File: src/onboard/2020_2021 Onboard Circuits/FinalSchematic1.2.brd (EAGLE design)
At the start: 135.6 x 80 mm, 97 parts, among them IC1 A5975D, IC2 A5975D, IC3 A5975D

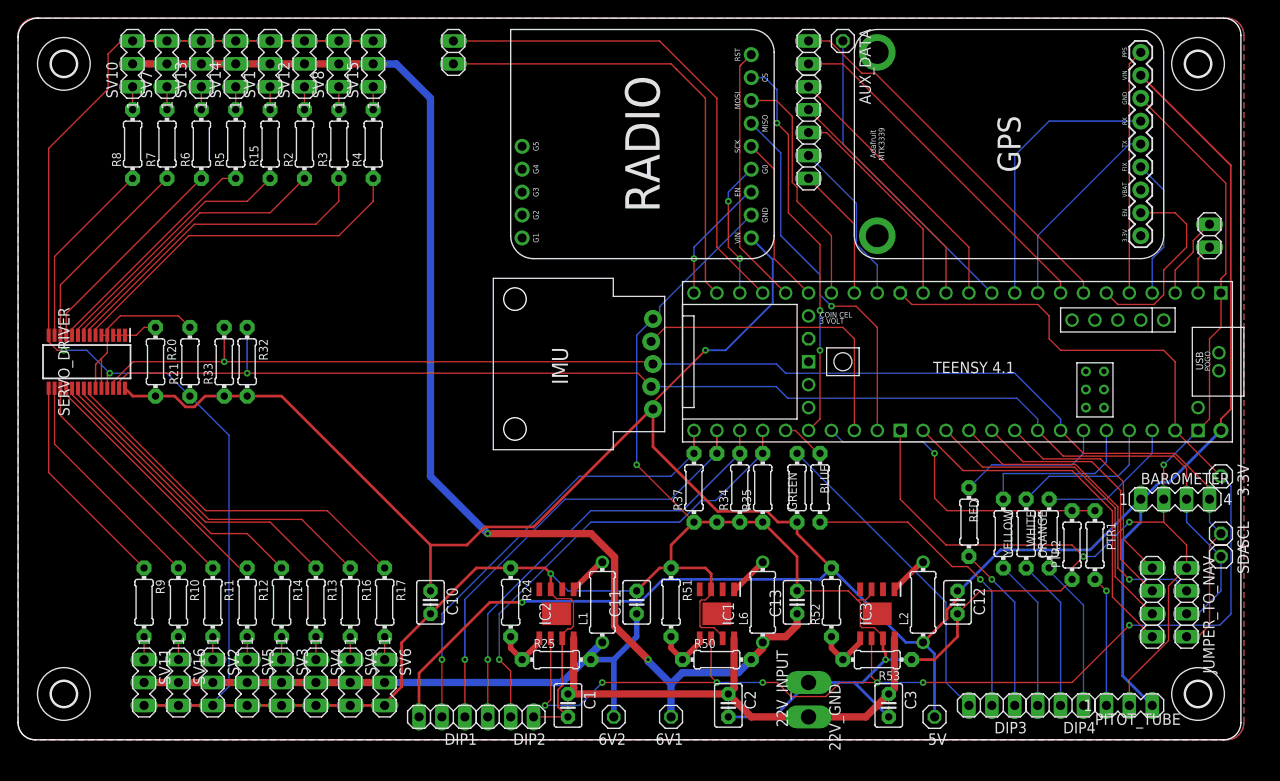
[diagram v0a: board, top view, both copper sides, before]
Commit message: Updated board using the jlcpcb2layer.dru file for DRC check. Added names next to pinheaders. Adjusted silkscreen of component names. Updated photos of baord and schematic.
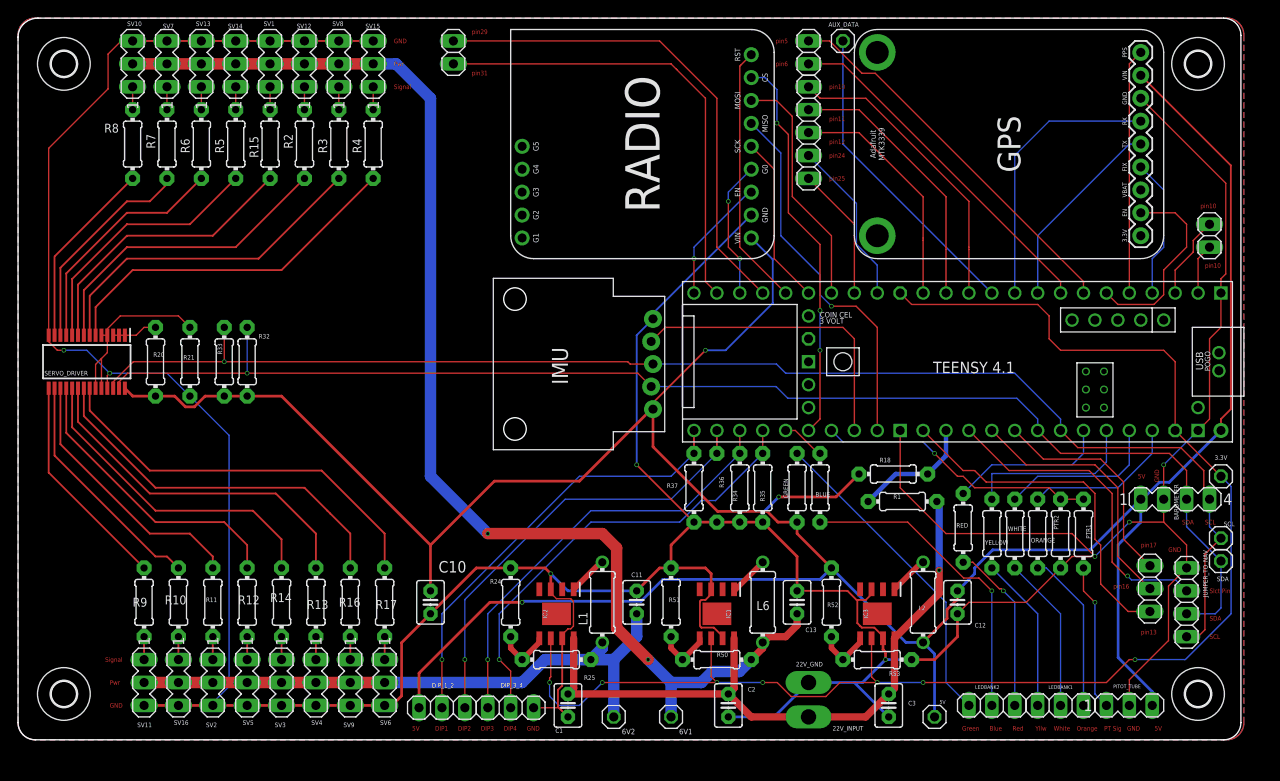
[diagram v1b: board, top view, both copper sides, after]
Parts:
- removed 3: (no value), pinhead:1X04
- removed DIP1, DIP2: (no value), pinhead:1X03
- added DIP_1_2, DIP_3_4, JP1: (no value), pinhead:1X03
- added R1: 1.8M, adafruit:0204/7
- added R18: 430k, adafruit:0204/7
- moved PTR1 1.80 mm to (82.5, 22.9)
- moved PTR2 1.80 mm to (80.0, 22.9)
- moved ORANGE 1.27 mm to (77.5, 22.9)
- moved WHITE 1.27 mm to (74.9, 22.9)
- moved YELLOW 1.27 mm to (72.4, 22.9)
- moved RED 0.90 mm to (69.2, 23.5)
- moved SCL 0.51 mm to (97.8, 22.4)
- moved SDA 0.51 mm to (97.8, 19.8)
- renumbered DIP3 to LEDBANK2, DIP4 to LEDBANK1
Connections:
- net 22_INPUT: now also R1.2
- net 5V: now also DIP_1_2.3; no longer DIP1.3
- net DIP1: now also DIP_1_2.2; no longer DIP1.2
- net DIP2: now also DIP_1_2.1; no longer DIP1.1
- net DIP3: now also DIP_3_4.3; no longer DIP2.3
- net DIP4: now also DIP_3_4.2; no longer DIP2.2
- net GND: now also DIP_3_4.1, R18.1; no longer DIP2.1
- net PIN13: now also JP1.3; no longer 3.4
- net PIN14: now also R1.1, R18.2; no longer 3.3
- net PIN16: now also JP1.2; no longer 3.2
- net PIN17: now also JP1.1; no longer 3.1
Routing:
- net OUTPUT_BUCK2: track 70.1 -> 94.7 mm
- net PIN14: track 35.7 -> 13.5 mm
- net 22_INPUT: track 57.0 -> 74.3 mm, vias 0 -> 1
- net GND: track 485.0 -> 499.1 mm, vias 8 -> 9
- net PT_ANLGPIN: track 35.8 -> 31.1 mm
- net PWM13: track 35.0 -> 39.0 mm
- net PWM12: track 31.9 -> 35.9 mm
- net PWM11: track 28.7 -> 32.7 mm
- net PWM14: track 38.2 -> 41.8 mm
- net PIN11: track 26.6 -> 29.9 mm
- net PWM15: track 41.4 -> 44.6 mm
- net PWM4: track 25.7 -> 29.0 mm
- net PIN10: track 30.2 -> 33.2 mm
- net PWM3: track 28.9 -> 31.8 mm
- net PWM10: track 26.9 -> 29.5 mm
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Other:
- board text added: "5V"
- board text added: "Blue"
- board text added: "DIP1"
- board text added: "DIP2"
- board text added: "DIP3"
- board text added: "DIP4"
- board text added: "GND"
- board text added: "Green"
- board text added: "Orange"
- board text added: "PT Sig"
- board text added: "Pwr"
- board text added: "Red"
- board text added: "SCL"
- board text added: "SDA"
- board text added: "Signal"
- board text added: "Slct Pin"
- board text added: "White"
- board text added: "Yllw"
- board text added: "pin10"
- board text added: "pin11"
- board text added: "pin12"
- board text added: "pin13"
- board text added: "pin16"
- board text added: "pin17"
- board text added: "pin24"
- board text added: "pin25"
- board text added: "pin29"
- board text added: "pin31"
- board text added: "pin5"
- board text added: "pin6"

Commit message: Changed Pinheader side names to Tplace on both boards
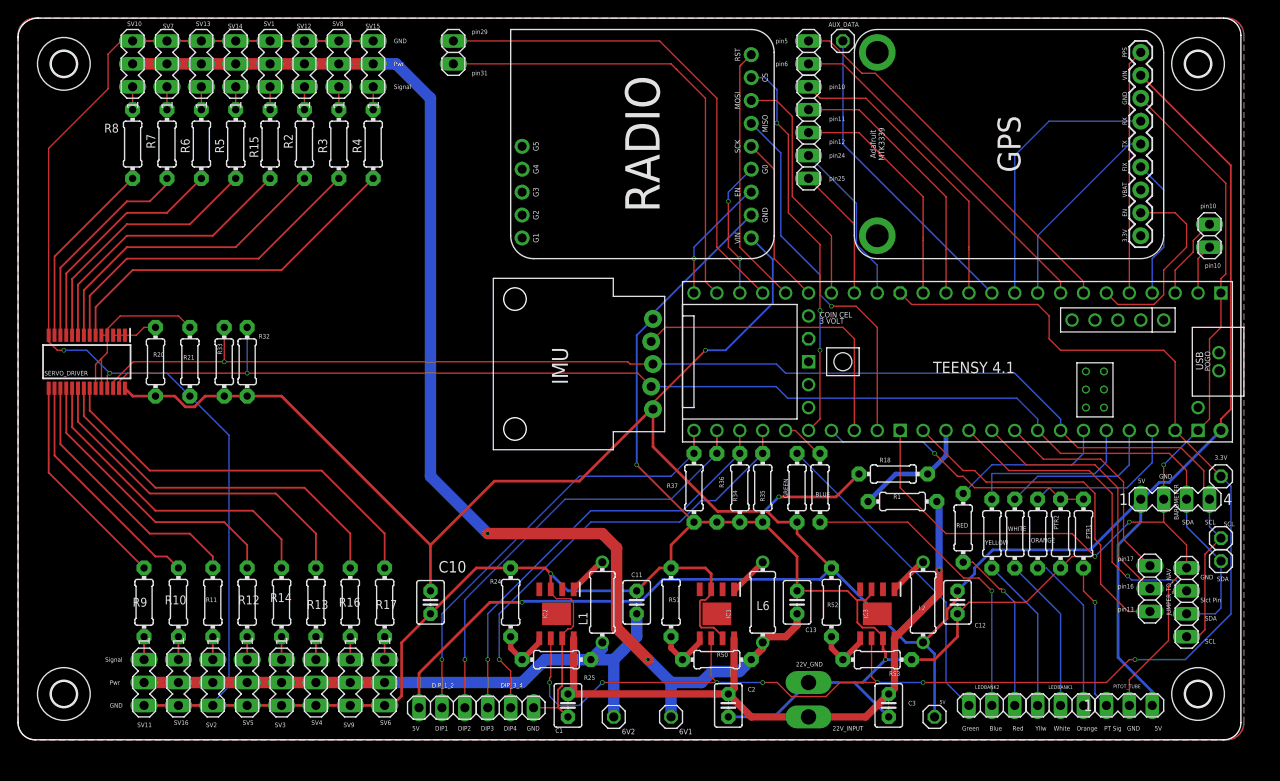
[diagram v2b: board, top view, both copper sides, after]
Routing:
- net O_LED: track 17.3 -> 17.9 mm
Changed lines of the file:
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@@
 <wire x1="-35.56" y1="77.90498125" x2="-35.56" y2="1.905" width="0" layer="20"/>
 <wire x1="-35.56" y1="1.905" x2="-33.655" y2="0" width="0" layer="20" curve="90"/>
-<text x="54.356" y="61.976" size="0.508" layer="1" font="vector">pin25</text>
-<text x="54.356" y="72.136" size="0.508" layer="1" font="vector">pin10</text>
-<text x="49.784" y="77.724" size="0.508" layer="1" font="vector" rot="R180">pin5</text>
-<text x="49.784" y="75.184" size="0.508" layer="1" font="vector" rot="R180">pin6</text>
-<text x="54.356" y="68.58" size="0.508" layer="1" font="vector">pin11</text>
-<text x="54.356" y="66.04" size="0.508" layer="1" font="vector">pin12</text>
-<text x="54.356" y="64.516" size="0.508" layer="1" font="vector">pin24</text>
-<text x="95.504" y="58.928" size="0.508" layer="1" font="vector">pin10</text>
-<text x="96.012" y="52.324" size="0.508" layer="1" font="vector">pin10</text>
-<text x="88.9" y="11.684" size="0.508" layer="1" font="vector">pin13</text>
-<text x="88.9" y="21.336" size="0.508" layer="1" font="vector">pin17</text>
-<text x="85.852" y="16.764" size="0.508" layer="1" font="vector">pin16</text>
-<text x="14.732" y="73.66" size="0.508" layer="1" font="vector">pin31</text>
-<text x="14.732" y="78.232" size="0.508" layer="1" font="vector">pin29</text>
-<text x="90.424" y="1.016" size="0.508" layer="1" font="vector">5V</text>
-<text x="87.376" y="1.016" size="0.508" layer="1" font="vector">GND</text>
-<text x="84.836" y="1.016" size="0.508" layer="1" font="vector">PT Sig</text>
-<text x="81.788" y="1.016" size="0.508" layer="1" font="vector">Orange</text>
-<text x="79.248" y="1.016" size="0.508" layer="1" font="vector">White</text>
-<text x="77.216" y="1.016" size="0.508" layer="1" font="vector">Yllw</text>
-<text x="74.676" y="1.016" size="0.508" layer="1" font="vector">Red</text>
-<text x="72.136" y="1.016" size="0.508" layer="1" font="vector">Blue</text>
-<text x="69.088" y="1.016" size="0.508" layer="1" font="vector">Green</text>
-<text x="96.52" y="11.176" size="0.508" layer="1" font="vector">SCL</text>
-<text x="96.52" y="13.208" size="0.508" layer="1" font="vector">SDA</text>
-<text x="96.52" y="16.256" size="0.508" layer="1" font="vector">Slct Pin</text>
-<text x="91.948" y="20.828" size="0.508" layer="1" font="vector">GND</text>
-<text x="20.828" y="1.016" size="0.508" layer="1" font="vector">GND</text>
-<text x="18.288" y="1.016" size="0.508" layer="1" font="vector">DIP4</text>
-<text x="15.748" y="1.016" size="0.508" layer="1" font="vector">DIP3</text>
-<text x="13.208" y="1.016" size="0.508" layer="1" font="vector">DIP2</text>
-<text x="10.668" y="1.016" size="0.508" layer="1" font="vector">DIP1</text>
-<text x="8.128" y="1.016" size="0.508" layer="1" font="vector">5V</text>
-<text x="-25.4" y="3.556" size="0.508" layer="1" font="vector">GND</text>
-<text x="-25.4" y="6.096" size="0.508" layer="1" font="vector">Pwr</text>
-<text x="-25.908" y="8.636" size="0.508" layer="1" font="vector">Signal</text>
-<text x="6.096" y="72.136" size="0.508" layer="1" font="vector">Signal</text>
-<text x="6.096" y="74.676" size="0.508" layer="1" font="vector">Pwr</text>
-<text x="6.096" y="77.216" size="0.508" layer="1" font="vector">GND</text>
-<text x="89.408" y="29.464" size="0.508" layer="1" font="vector" rot="R180">5V</text>
-<text x="93.472" y="23.876" size="0.508" layer="1" font="vector">SDA</text>
-<text x="96.012" y="23.876" size="0.508" layer="1" font="vector">SCL</text>
-<text x="90.424" y="29.972" size="0.508" layer="1" font="vector" rot="R270">GND</text>
+<text x="54.356" y="61.976" size="0.508" layer="21" font="vector">pin25</text>
+<text x="54.356" y="72.136" size="0.508" layer="21" font="vector">pin10</text>
+<text x="49.784" y="77.724" size="0.508" layer="21" font="vector" rot="R180">pin5</text>
+<text x="49.784" y="75.184" size="0.508" layer="21" font="vector" rot="R180">pin6</text>
+<text x="54.356" y="68.58" size="0.508" layer="21" font="vector">pin11</text>
+<text x="54.356" y="66.04" size="0.508" layer="21" font="vector">pin12</text>
+<text x="54.356" y="64.516" size="0.508" layer="21" font="vector">pin24</text>
+<text x="95.504" y="58.928" size="0.508" layer="21" font="vector">pin10</text>
+<text x="96.012" y="52.324" size="0.508" layer="21" font="vector">pin10</text>
+<text x="86.36" y="14.224" size="0.508" layer="21" font="vector">pin13</text>
+<text x="86.36" y="19.812" size="0.508" layer="21" font="vector">pin17</text>
+<text x="86.36" y="16.764" size="0.508" layer="21" font="vector">pin16</text>
+<text x="14.732" y="73.66" size="0.508" layer="21" font="vector">pin31</text>
+<text x="14.732" y="78.232" size="0.508" layer="21" font="vector">pin29</text>
+<text x="90.424" y="1.016" size="0.508" layer="21" font="vector">5V</text>
+<text x="87.376" y="1.016" size="0.508" layer="21" font="vector">GND</text>
+<text x="84.836" y="1.016" size="0.508" layer="21" font="vector">PT Sig</text>
+<text x="81.788" y="1.016" size="0.508" layer="21" font="vector">Orange</text>
+<text x="79.248" y="1.016" size="0.508" layer="21" font="vector">White</text>
+<text x="77.216" y="1.016" size="0.508" layer="21" font="vector">Yllw</text>
+<text x="74.676" y="1.016" size="0.508" layer="21" font="vector">Red</text>
+<text x="72.136" y="1.016" size="0.508" layer="21" font="vector">Blue</text>
+<text x="69.088" y="1.016" size="0.508" layer="21" font="vector">Green</text>
+<text x="96.012" y="10.668" size="0.508" layer="21" font="vector">SCL</text>
+<text x="96.012" y="13.208" size="0.508" layer="21" font="vector">SDA</text>
+<text x="95.504" y="15.24" size="0.508" layer="21" font="vector">Slct Pin</text>
+<text x="95.504" y="17.78" size="0.508" layer="21" font="vector">GND</text>
+<text x="20.828" y="1.016" size="0.508" layer="21" font="vector">GND</text>
+<text x="18.288" y="1.016" size="0.508" layer="21" font="vector">DIP4</text>
+<text x="15.748" y="1.016" size="0.508" layer="21" font="vector">DIP3</text>
+<text x="13.208" y="1.016" size="0.508" layer="21" font="vector">DIP2</text>
+<text x="10.668" y="1.016" size="0.508" layer="21" font="vector">DIP1</text>
+<text x="8.128" y="1.016" size="0.508" layer="21" font="vector">5V</text>
+<text x="-25.4" y="3.556" size="0.508" layer="21" font="vector">GND</text>
+<text x="-25.4" y="6.096" size="0.508" layer="21" font="vector">Pwr</text>
+<text x="-25.908" y="8.636" size="0.508" layer="21" font="vector">Signal</text>
+<text x="6.096" y="72.136" size="0.508" layer="21" font="vector">Signal</text>
+<text x="6.096" y="74.676" size="0.508" layer="21" font="vector">Pwr</text>
+<text x="6.096" y="77.216" size="0.508" layer="21" font="vector">GND</text>
+<text x="89.408" y="28.956" size="0.508" layer="21" font="vector" rot="R180">5V</text>
+<text x="93.472" y="23.876" size="0.508" layer="21" font="vector">SDA</text>
+<text x="96.012" y="23.876" size="0.508" layer="21" font="vector">SCL</text>
+<text x="90.932" y="28.956" size="0.508" layer="21" font="vector">GND</text>
 </plain>
 <attributes>
@@
 </element>
 <element name="JUMPER_TO_NAV" library="pinhead" library_urn="urn:adsk.eagle:library:325" package="1X04" package3d_urn="urn:adsk.eagle:package:22407/2" value="" x="93.98" y="15.24" smashed="yes" rot="R270">
-<attribute name="NAME" x="95.8088" y="21.0312" size="0.508" layer="25" ratio="10" rot="R270"/>
+<attribute name="NAME" x="91.7448" y="18.9992" size="0.508" layer="25" ratio="10" rot="R270"/>
 <attribute name="POPULARITY" value="91" x="93.98" y="15.24" size="1.778" layer="27" rot="R270" display="off"/>
 <attribute name="VALUE" x="90.805" y="20.32" size="1.27" layer="27" rot="R270"/>
@@
 <wire x1="58.0672" y1="6.35" x2="60.6072" y2="8.89" width="0.3048" layer="16"/>
 <wire x1="40.0306" y1="12.59926875" x2="40.0306" y2="12.7" width="0.1524" layer="1"/>
-<wire x1="57.810934375" y1="12.598934375" x2="57.8106" y2="12.59926875" width="0.1524" layer="1"/>
 <wire x1="87.63" y1="24.13" x2="83.82" y2="20.32" width="0.1524" layer="16"/>
 <via x="83.82" y="20.32" extent="1-16" drill="0.35"/>
@@
 <wire x1="50.8" y1="16.51" x2="56.388" y2="16.51" width="0.2032" layer="1"/>
 <wire x1="58.42" y1="15.5044" x2="57.47996875" y2="15.5044" width="0.2032" layer="1"/>
-<wire x1="57.47996875" y1="15.5044" x2="57.47996875" y2="12.9299" width="0.2032" layer="1"/>
-<wire x1="57.47996875" y1="12.9299" x2="57.810934375" y2="12.598934375" width="0.2032" layer="1"/>
-<wire x1="57.97426875" y1="12.4356" x2="57.810934375" y2="12.598934375" width="0.2032" layer="1"/>
-<wire x1="57.97426875" y1="12.4356" x2="59.36003125" y2="12.4356" width="0.2032" layer="1"/>
 <wire x1="59.36003125" y1="12.4356" x2="60.325" y2="11.47063125" width="0.2032" layer="1"/>
 <wire x1="60.325" y1="11.47063125" x2="60.325" y2="11.258" width="0.2032" layer="1"/>
@@
 <wire x1="40.64" y1="15.5044" x2="41.275" y2="16.1394" width="0.2032" layer="1"/>
 <wire x1="41.275" y1="16.1394" x2="41.275" y2="16.682" width="0.2032" layer="1"/>
+<wire x1="57.47996875" y1="15.5044" x2="57.47996875" y2="13.00174375" width="0.2032" layer="1"/>
+<wire x1="57.47996875" y1="13.00174375" x2="58.0461125" y2="12.4356" width="0.2032" layer="1"/>
+<wire x1="58.0461125" y1="12.4356" x2="59.36003125" y2="12.4356" width="0.2032" layer="1"/>
 </signal>
 <signal name="GPS_EN">
@@
 <contactref element="ORANGE" pad="1"/>
 <contactref element="TEENSY4.1" pad="23-A9/CRX1/MCLK1"/>
-<wire x1="90.17" y1="34.29" x2="90.17" y2="31.75" width="0.1524" layer="16"/>
-<wire x1="86.36" y1="27.94" x2="78.74" y2="27.94" width="0.1524" layer="16"/>
+<wire x1="90.17" y1="34.29" x2="90.17" y2="30.734" width="0.1524" layer="16"/>
+<wire x1="87.376" y1="27.94" x2="78.74" y2="27.94" width="0.1524" layer="16"/>
 <wire x1="78.74" y1="27.94" x2="77.47" y2="26.67" width="0.1524" layer="16"/>
-<wire x1="90.17" y1="31.75" x2="86.36" y2="27.94" width="0.1524" layer="16"/>
+<wire x1="90.17" y1="30.734" x2="87.376" y2="27.94" width="0.1524" layer="16"/>
 </signal>
 <signal name="ORANGE">
